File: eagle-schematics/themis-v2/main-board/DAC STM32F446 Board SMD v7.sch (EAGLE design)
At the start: 275 parts, among them Q1 16MHz

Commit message: Bug fix
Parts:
- C35: value 1p -> 100p
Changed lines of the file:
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@@
 <setting verticaltext="up"/>
 </settings>
-<grid distance="0.05" unitdist="inch" unit="inch" style="lines" multiple="1" display="no" altdistance="0.01" altunitdist="inch" altunit="inch"/>
+<grid distance="0.1" unitdist="inch" unit="inch" style="lines" multiple="1" display="no" altdistance="0.01" altunitdist="inch" altunit="inch"/>
 <layers>
-<layer number="1" name="Top" color="4" fill="1" visible="yes" active="no"/>
-<layer number="2" name="Route2" color="1" fill="3" visible="yes" active="no"/>
-<layer number="3" name="Route3" color="4" fill="3" visible="yes" active="no"/>
-<layer number="4" name="Route4" color="1" fill="4" visible="yes" active="no"/>
-<layer number="5" name="Route5" color="4" fill="4" visible="yes" active="no"/>
-<layer number="6" name="Route6" color="1" fill="8" visible="yes" active="no"/>
-<layer number="7" name="Route7" color="4" fill="8" visible="yes" active="no"/>
-<layer number="8" name="Route8" color="1" fill="2" visible="yes" active="no"/>
-<layer number="9" name="Route9" color="4" fill="2" visible="yes" active="no"/>
-<layer number="10" name="Route10" color="1" fill="7" visible="yes" active="no"/>
-<layer number="11" name="Route11" color="4" fill="7" visible="yes" active="no"/>
-<layer number="12" name="Route12" color="1" fill="5" visible="yes" active="no"/>
-<layer number="13" name="Route13" color="4" fill="5" visible="yes" active="no"/>
-<layer number="14" name="Route14" color="1" fill="6" visible="yes" active="no"/>
-<layer number="15" name="Route15" color="4" fill="6" visible="yes" active="no"/>
-<layer number="16" name="Bottom" color="1" fill="1" visible="yes" active="no"/>
-<layer number="17" name="Pads" color="2" fill="1" visible="yes" active="no"/>
-<layer number="18" name="Vias" color="2" fill="1" visible="yes" active="no"/>
-<layer number="19" name="Unrouted" color="6" fill="1" visible="yes" active="no"/>
-<layer number="20" name="Dimension" color="24" fill="1" visible="yes" active="no"/>
-<layer number="21" name="tPlace" color="7" fill="1" visible="yes" active="no"/>
-<layer number="22" name="bPlace" color="7" fill="1" visible="yes" active="no"/>
-<layer number="23" name="tOrigins" color="15" fill="1" visible="yes" active="no"/>
-<layer number="24" name="bOrigins" color="15" fill="1" visible="yes" active="no"/>
-<layer number="25" name="tNames" color="7" fill="1" visible="yes" active="no"/>
-<layer number="26" name="bNames" color="7" fill="1" visible="yes" active="no"/>
-<layer number="27" name="tValues" color="7" fill="1" visible="yes" active="no"/>
-<layer number="28" name="bValues" color="7" fill="1" visible="yes" active="no"/>
+<layer number="1" name="Top" color="4" fill="1" visible="no" active="no"/>
+<layer number="2" name="Route2" color="1" fill="3" visible="no" active="no"/>
+<layer number="3" name="Route3" color="4" fill="3" visible="no" active="no"/>
+<layer number="4" name="Route4" color="1" fill="4" visible="no" active="no"/>
+<layer number="5" name="Route5" color="4" fill="4" visible="no" active="no"/>
+<layer number="6" name="Route6" color="1" fill="8" visible="no" active="no"/>
+<layer number="7" name="Route7" color="4" fill="8" visible="no" active="no"/>
+<layer number="8" name="Route8" color="1" fill="2" visible="no" active="no"/>
+<layer number="9" name="Route9" color="4" fill="2" visible="no" active="no"/>
+<layer number="10" name="Route10" color="1" fill="7" visible="no" active="no"/>
+<layer number="11" name="Route11" color="4" fill="7" visible="no" active="no"/>
+<layer number="12" name="Route12" color="1" fill="5" visible="no" active="no"/>
+<layer number="13" name="Route13" color="4" fill="5" visible="no" active="no"/>
+<layer number="14" name="Route14" color="1" fill="6" visible="no" active="no"/>
+<layer number="15" name="Route15" color="4" fill="6" visible="no" active="no"/>
+<layer number="16" name="Bottom" color="1" fill="1" visible="no" active="no"/>
+<layer number="17" name="Pads" color="2" fill="1" visible="no" active="no"/>
+<layer number="18" name="Vias" color="2" fill="1" visible="no" active="no"/>
+<layer number="19" name="Unrouted" color="6" fill="1" visible="no" active="no"/>
+<layer number="20" name="Dimension" color="24" fill="1" visible="no" active="no"/>
+<layer number="21" name="tPlace" color="7" fill="1" visible="no" active="no"/>
+<layer number="22" name="bPlace" color="7" fill="1" visible="no" active="no"/>
+<layer number="23" name="tOrigins" color="15" fill="1" visible="no" active="no"/>
+<layer number="24" name="bOrigins" color="15" fill="1" visible="no" active="no"/>
+<layer number="25" name="tNames" color="7" fill="1" visible="no" active="no"/>
+<layer number="26" name="bNames" color="7" fill="1" visible="no" active="no"/>
+<layer number="27" name="tValues" color="7" fill="1" visible="no" active="no"/>
+<layer number="28" name="bValues" color="7" fill="1" visible="no" active="no"/>
 <layer number="29" name="tStop" color="7" fill="3" visible="no" active="no"/>
 <layer number="30" name="bStop" color="7" fill="6" visible="no" active="no"/>
@@
 <layer number="35" name="tGlue" color="7" fill="4" visible="no" active="no"/>
 <layer number="36" name="bGlue" color="7" fill="5" visible="no" active="no"/>
-<layer number="37" name="tTest" color="7" fill="1" visible="yes" active="no"/>
-<layer number="38" name="bTest" color="7" fill="1" visible="yes" active="no"/>
+<layer number="37" name="tTest" color="7" fill="1" visible="no" active="no"/>
+<layer number="38" name="bTest" color="7" fill="1" visible="no" active="no"/>
 <layer number="39" name="tKeepout" color="4" fill="11" visible="no" active="no"/>
 <layer number="40" name="bKeepout" color="1" fill="11" visible="no" active="no"/>
@@
 <layer number="44" name="Drills" color="7" fill="1" visible="no" active="no"/>
 <layer number="45" name="Holes" color="7" fill="1" visible="no" active="no"/>
-<layer number="46" name="Milling" color="3" fill="1" visible="yes" active="no"/>
-<layer number="47" name="Measures" color="7" fill="1" visible="yes" active="no"/>
-<layer number="48" name="Document" color="7" fill="1" visible="yes" active="no"/>
-<layer number="49" name="Reference" color="7" fill="1" visible="yes" active="no"/>
-<layer number="50" name="dxf" color="7" fill="1" visible="yes" active="no"/>
-<layer number="51" name="tDocu" color="7" fill="1" visible="yes" active="no"/>
-<layer number="52" name="bDocu" color="7" fill="1" visible="yes" active="no"/>
-<layer number="53" name="tGND_GNDA" color="7" fill="9" visible="yes" active="no"/>
-<layer number="54" name="bGND_GNDA" color="1" fill="9" visible="yes" active="no"/>
-<layer number="56" name="wert" color="7" fill="1" visible="yes" active="no"/>
-<layer number="57" name="tCAD" color="7" fill="1" visible="yes" active="no"/>
+<layer number="46" name="Milling" color="3" fill="1" visible="no" active="no"/>
+<layer number="47" name="Measures" color="7" fill="1" visible="no" active="no"/>
+<layer number="48" name="Document" color="7" fill="1" visible="no" active="no"/>
+<layer number="49" name="Reference" color="7" fill="1" visible="no" active="no"/>
+<layer number="50" name="dxf" color="7" fill="1" visible="no" active="no"/>
+<layer number="51" name="tDocu" color="7" fill="1" visible="no" active="no"/>
+<layer number="52" name="bDocu" color="7" fill="1" visible="no" active="no"/>
+<layer number="53" name="tGND_GNDA" color="7" fill="9" visible="no" active="no"/>
+<layer number="54" name="bGND_GNDA" color="1" fill="9" visible="no" active="no"/>
+<layer number="56" name="wert" color="7" fill="1" visible="no" active="no"/>
+<layer number="57" name="tCAD" color="7" fill="1" visible="no" active="no"/>
 <layer number="58" name="bCAD" color="7" fill="1" visible="no" active="no"/>
-<layer number="59" name="tCarbon" color="7" fill="1" visible="yes" active="no"/>
-<layer number="60" name="bCarbon" color="7" fill="1" visible="yes" active="no"/>
+<layer number="59" name="tCarbon" color="7" fill="1" visible="no" active="no"/>
+<layer number="60" name="bCarbon" color="7" fill="1" visible="no" active="no"/>
 <layer number="88" name="SimResults" color="9" fill="1" visible="yes" active="yes"/>
 <layer number="89" name="SimProbes" color="9" fill="1" visible="yes" active="yes"/>
@@
 <part name="ITOV" library="linear" library_urn="urn:adsk.eagle:library:262" deviceset="NE5534" device="N" package3d_urn="urn:adsk.eagle:package:16409/2" technology="A" value="NE5534AN"/>
 <part name="R48" library="rcl" library_urn="urn:adsk.eagle:library:334" deviceset="R-EU_" device="R0805" package3d_urn="urn:adsk.eagle:package:23553/2" value="33K"/>
-<part name="C35" library="rcl" library_urn="urn:adsk.eagle:library:334" deviceset="C-EU" device="C0805" package3d_urn="urn:adsk.eagle:package:23617/2" value="1p">
-<spice>
-<pinmapping spiceprefix="C">
+<part name="C35" library="rcl" library_urn="urn:adsk.eagle:library:334" deviceset="C-EU" device="C0805" package3d_urn="urn:adsk.eagle:package:23617/2" value="100p">
+<spice>
+<pinmapping spiceprefix="C">

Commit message: fixed pol cap and LED orientation errors
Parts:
- R89, R91: value 330 -> 180
- R90, R95: value 330 -> 1k
- R92: value 330 -> 470
- R93, R94: value 330 -> 10k
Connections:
- net -15V: now also C54.-; no longer C54.+
- net GND: now also -15V.A, C54.+; no longer -15V.C, C54.-
- net N$54: now also -15V.C; no longer -15V.A
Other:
- note added: "!!!! Erreurs de routage à corriger !!!! Au moment de l'équipement de la carte : - inverser le condo polarisé C54 (+ côté 0V et non côté -15V) - inverser la LED "-15V" (pour la même raison)"
- moved on the sheet: -15V, C54, R93

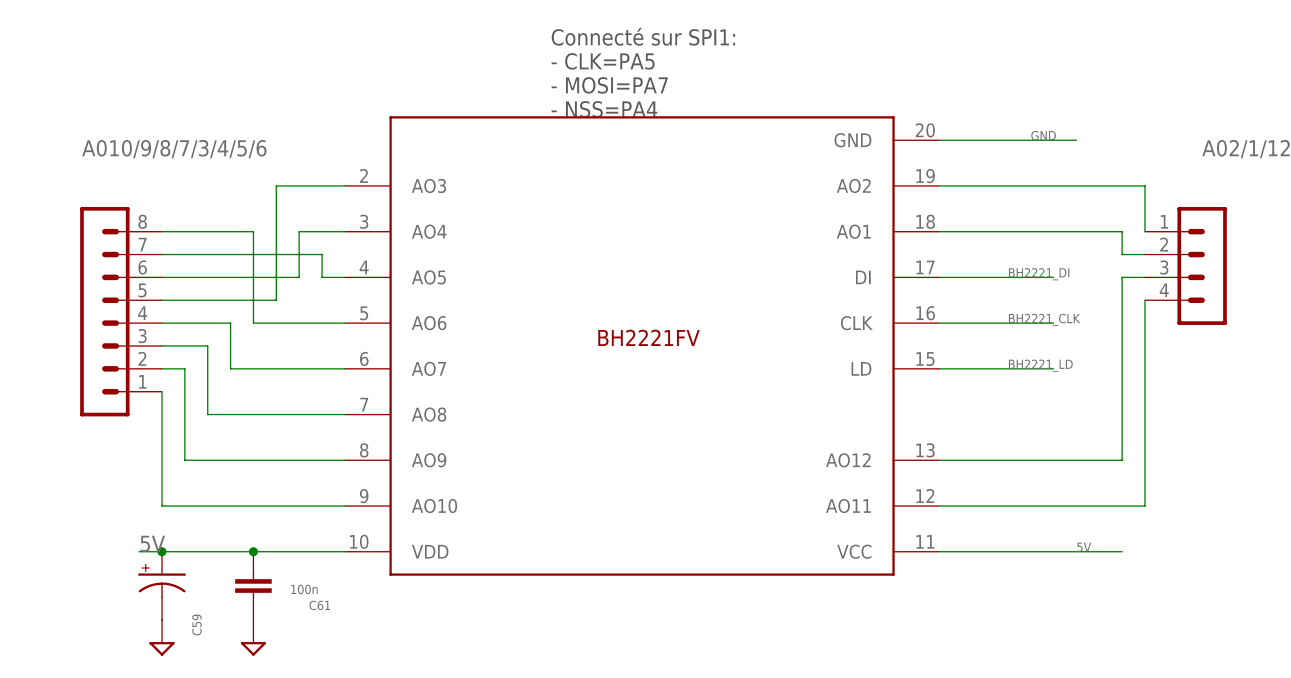
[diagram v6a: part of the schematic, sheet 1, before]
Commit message: Updated net names
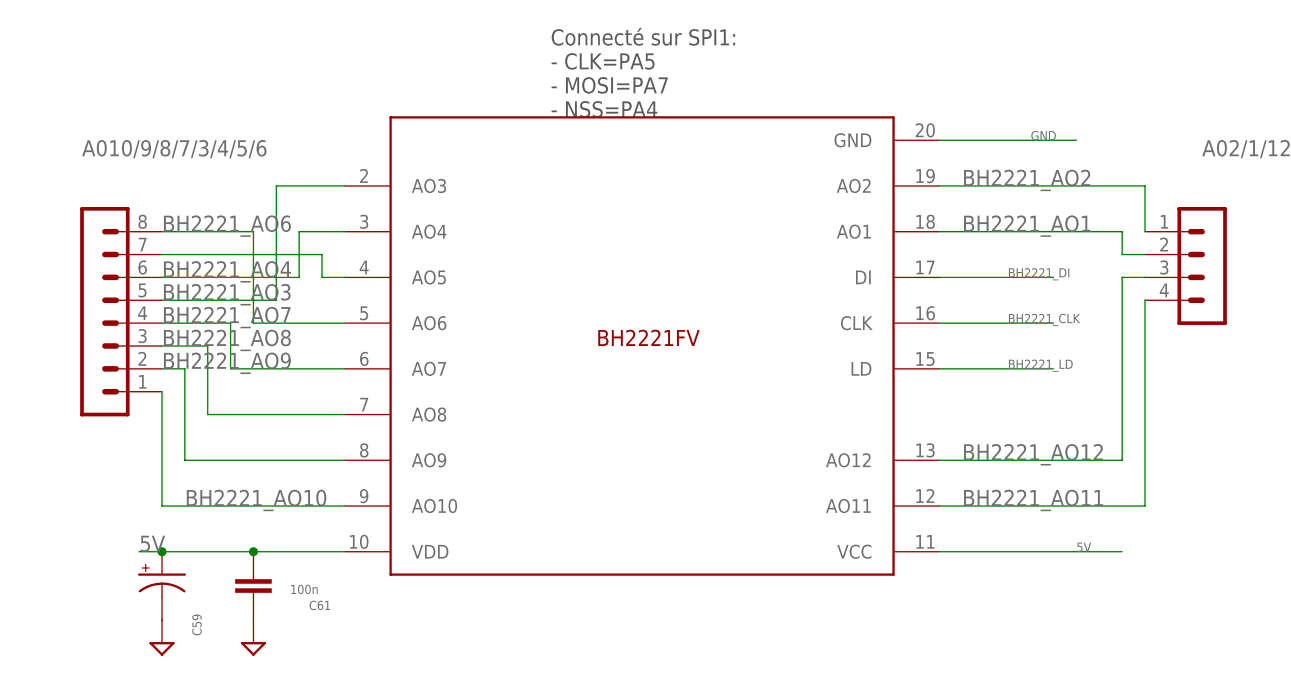
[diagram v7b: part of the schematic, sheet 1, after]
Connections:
- net N$19 renamed BH2221_AO3
- net N$21 renamed BH2221_AO4
- net N$25 renamed BH2221_AO6
- net N$26 renamed BH2221_AO7
- net N$27 renamed BH2221_AO8
- net N$28 renamed BH2221_AO9
- net N$29 renamed BH2221_AO10
- net N$30 renamed BH2221_AO2
- net N$31 renamed BH2221_AO1
- net N$32 renamed BH2221_AO12
- net N$33 renamed BH2221_AO11
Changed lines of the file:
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@@
 </segment>
 </net>
-<net name="N$26" class="0">
+<net name="BH2221_AO7" class="0">
 <segment>
 <pinref part="A010/9/8/7/3/4/5/6" gate="1" pin="4"/>
@@
 <pinref part="BH2221" gate="G$1" pin="AO7"/>
 <wire x1="495.3" y1="233.68" x2="508" y2="233.68" width="0.1524" layer="91"/>
-</segment>
-</net>
-<net name="N$27" class="0">
+<label x="487.68" y="238.76" size="1.778" layer="95"/>
+</segment>
+</net>
+<net name="BH2221_AO8" class="0">
 <segment>
 <pinref part="A010/9/8/7/3/4/5/6" gate="1" pin="3"/>
@@
 <wire x1="492.76" y1="236.22" x2="492.76" y2="228.6" width="0.1524" layer="91"/>
 <wire x1="492.76" y1="228.6" x2="508" y2="228.6" width="0.1524" layer="91"/>
-</segment>
-</net>
-<net name="N$28" class="0">
+<label x="487.68" y="236.22" size="1.778" layer="95"/>
+</segment>
+</net>
+<net name="BH2221_AO9" class="0">
 <segment>
 <pinref part="A010/9/8/7/3/4/5/6" gate="1" pin="2"/>
@@
 <pinref part="BH2221" gate="G$1" pin="AO9"/>
 <wire x1="490.22" y1="223.52" x2="508" y2="223.52" width="0.1524" layer="91"/>
-</segment>
-</net>
-<net name="N$29" class="0">
+<label x="487.68" y="233.68" size="1.778" layer="95"/>
+</segment>
+</net>
+<net name="BH2221_AO10" class="0">
 <segment>
 <pinref part="A010/9/8/7/3/4/5/6" gate="1" pin="1"/>
@@
 <pinref part="BH2221" gate="G$1" pin="AO10"/>
 <wire x1="487.68" y1="218.44" x2="508" y2="218.44" width="0.1524" layer="91"/>
-</segment>
-</net>
-<net name="N$30" class="0">
+<label x="490.22" y="218.44" size="1.778" layer="95"/>
+</segment>
+</net>
+<net name="BH2221_AO2" class="0">
 <segment>
 <pinref part="BH2221" gate="G$1" pin="AO2"/>
@@
 <pinref part="A02/1/12/11" gate="1" pin="1"/>
 <wire x1="596.9" y1="254" x2="596.9" y2="248.92" width="0.1524" layer="91"/>
-</segment>
-</net>
-<net name="N$31" class="0">
+<label x="576.58" y="254" size="1.778" layer="95"/>
+</segment>
+</net>
+<net name="BH2221_AO1" class="0">
 <segment>
 <pinref part="BH2221" gate="G$1" pin="AO1"/>
@@
 <pinref part="A02/1/12/11" gate="1" pin="2"/>
 <wire x1="594.36" y1="246.38" x2="596.9" y2="246.38" width="0.1524" layer="91"/>
-</segment>
-</net>
-<net name="N$32" class="0">
+<label x="576.58" y="248.92" size="1.778" layer="95"/>
+</segment>
+</net>
+<net name="BH2221_AO12" class="0">
 <segment>
 <pinref part="BH2221" gate="G$1" pin="AO12"/>
@@
 <pinref part="A02/1/12/11" gate="1" pin="3"/>
 <wire x1="594.36" y1="243.84" x2="596.9" y2="243.84" width="0.1524" layer="91"/>
-</segment>
-</net>
-<net name="N$33" class="0">
+<label x="576.58" y="223.52" size="1.778" layer="95"/>
+</segment>
+</net>
+<net name="BH2221_AO11" class="0">
 <segment>
 <pinref part="A02/1/12/11" gate="1" pin="4"/>
@@
 <pinref part="BH2221" gate="G$1" pin="AO11"/>
 <wire x1="596.9" y1="218.44" x2="574.04" y2="218.44" width="0.1524" layer="91"/>
+<label x="576.58" y="218.44" size="1.778" layer="95"/>
 </segment>
 </net>
@@
 </segment>
 </net>
-<net name="N$19" class="0">
+<net name="BH2221_AO3" class="0">
 <segment>
 <pinref part="A010/9/8/7/3/4/5/6" gate="1" pin="5"/>
@@
 <wire x1="500.38" y1="241.3" x2="500.38" y2="254" width="0.1524" layer="91"/>
 <wire x1="500.38" y1="254" x2="508" y2="254" width="0.1524" layer="91"/>
-</segment>
-</net>
-<net name="N$21" class="0">
+<label x="487.68" y="241.3" size="1.778" layer="95"/>
+</segment>
+</net>
+<net name="BH2221_AO4" class="0">
 <segment>
 <pinref part="A010/9/8/7/3/4/5/6" gate="1" pin="6"/>
@@
 <pinref part="BH2221" gate="G$1" pin="AO4"/>
 <wire x1="502.92" y1="248.92" x2="508" y2="248.92" width="0.1524" layer="91"/>
+<label x="487.68" y="243.84" size="1.778" layer="95"/>
 </segment>
 </net>
@@
 </segment>
 </net>
-<net name="N$25" class="0">
+<net name="BH2221_AO6" class="0">
 <segment>
 <pinref part="BH2221" gate="G$1" pin="AO6"/>
@@
 <pinref part="A010/9/8/7/3/4/5/6" gate="1" pin="8"/>
 <wire x1="497.84" y1="248.92" x2="487.68" y2="248.92" width="0.1524" layer="91"/>
-</segment>
-</net>
+<label x="487.68" y="248.92" size="1.778" layer="95"/>
+</segment>
+</net>
